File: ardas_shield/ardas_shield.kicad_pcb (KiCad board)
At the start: 2 copper layers, 68.6 x 53.3 mm, 40 parts, among them CON1 SD_Card, IC1 DS1307, P1 CONN_10, P10 CONN_01X03, P2 CONN_8, P3 CONN_8, P4 CONN_ICSP, P5 CONN_6, P6 TTL_COMM, P7 CONN_01X03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

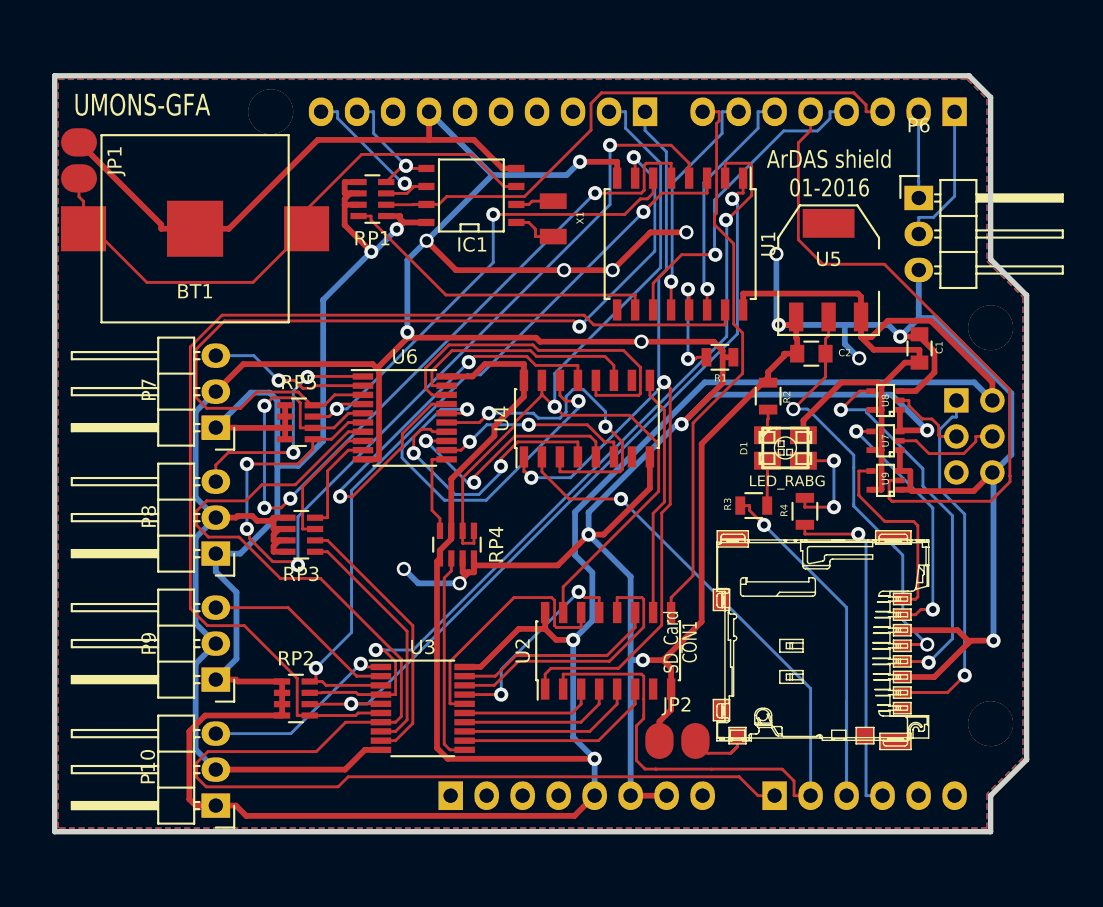
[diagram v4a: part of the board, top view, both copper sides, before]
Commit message: updated SD card and RGB-LED
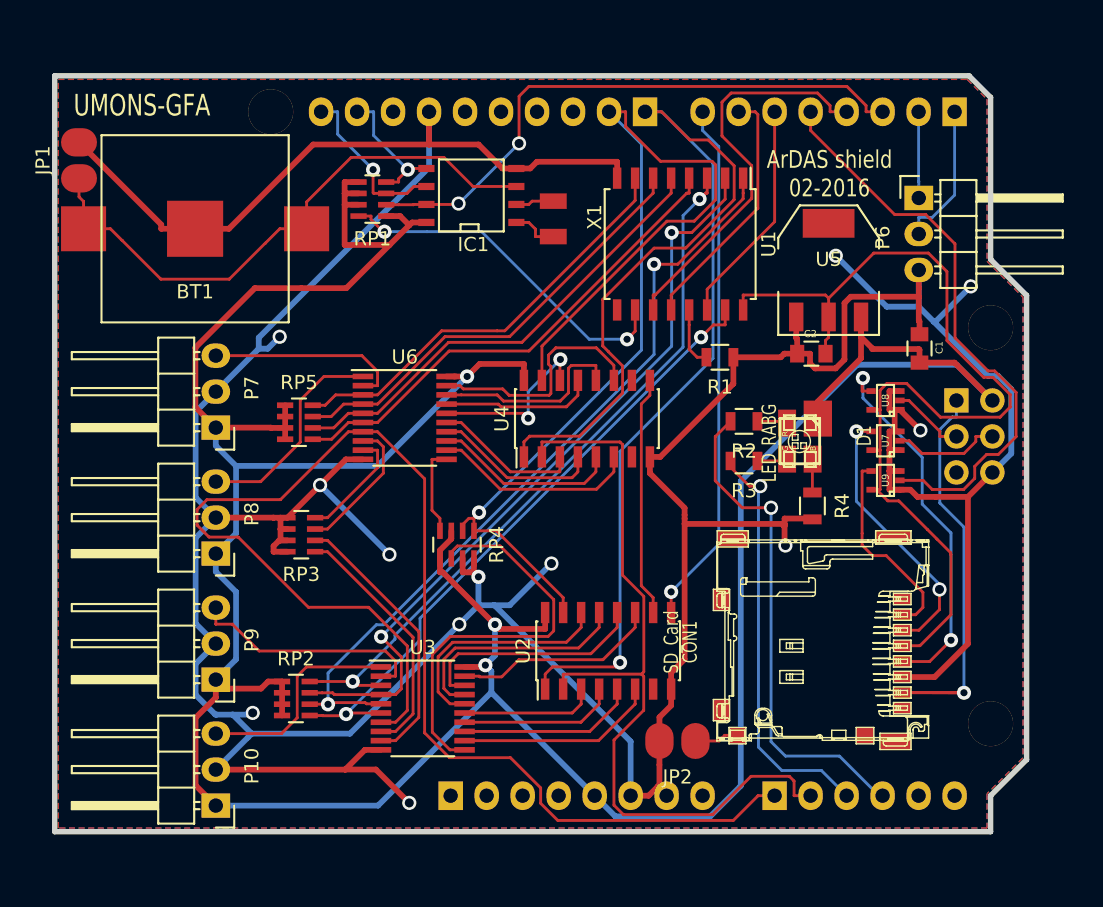
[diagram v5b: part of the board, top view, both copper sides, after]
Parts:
- BT1: footprint MyFootprints:BATTERY_KEYSTONE_12mm -> kicad-gfa local:BATTERY_KEYSTONE_12mm
- C1, C2: footprint Capacitors_SMD:C_0805 -> kicad-gfa local:C_0805
- D1: footprint MyFootprints:led-P-LCC-4-3 -> kicad-gfa local:led-P-LCC-4-3
- IC1: footprint SMD_Packages:SOIC-8-N -> kicad-gfa local:SOIC-8-N
- JP1, JP2: footprint RTC_Ardas_test:small_no_jumper -> kicad-gfa local:small_no_jumper
- P1: footprint Pin_Headers:Pin_Header_Straight_1x10 -> kicad-gfa local:Pin_Header_Straight_1x10
- P10, P6, P7, P8, P9: footprint Pin_Headers:Pin_Header_Angled_1x03 -> kicad-gfa local:Pin_Header_Angled_1x03
- P2, P3: footprint Pin_Headers:Pin_Header_Straight_1x08 -> kicad-gfa local:Pin_Header_Straight_1x08
- P4: footprint Socket_Strips:Socket_Strip_Straight_2x03 -> kicad-gfa local:Socket_Strip_Straight_2x03
- P5: footprint Pin_Headers:Pin_Header_Straight_1x06 -> kicad-gfa local:Pin_Header_Straight_1x06
- R1: footprint Resistors_SMD:R_0805 -> kicad-gfa local:R_0805
- R2: value 150 -> 4.7k; footprint Ardas_shield:R_0805 -> kicad-gfa local:R_0805
- R3: value 100 -> 10k; footprint Ardas_shield:R_0805 -> kicad-gfa local:R_0805
- R4: value 100 -> 4.7k; footprint Ardas_shield:R_0805 -> kicad-gfa local:R_0805
- U1: footprint Housings_SOIC:SOIC-16_7.5x10.3mm_Pitch1.27mm -> kicad-gfa local:SOIC-16_7.5x10.3mm_Pitch1.27mm
- U2, U4: footprint Housings_SOIC:SOIC-16_3.9x9.9mm_Pitch1.27mm -> kicad-gfa local:SOIC-16_3.9x9.9mm_Pitch1.27mm
- U3, U6: footprint Housings_SSOP:TSSOP-20_4.4x6.5mm_Pitch0.65mm -> kicad-gfa local:TSSOP-20_4.4x6.5mm_Pitch0.65mm
- U5: footprint TO_SOT_Packages_SMD:SOT-223 -> kicad-gfa local:SOT-223
- U7, U8, U9: footprint TO_SOT_Packages_SMD:SC-70-5 -> kicad-gfa local:SC-70-5
- X1: footprint MyFootprints:XTAL_ABRACON_ABS07 -> kicad-gfa local:XTAL_ABRACON_ABS07
- moved R3 3.22 mm to (95.7, 95.4)
- moved R2 2.46 mm to (95.7, 92.6), turned to 180 degrees
- moved D1 1.12 mm to (99.6, 94.0), turned to 180 degrees
- moved R4 0.66 mm to (100.5, 98.5)
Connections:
- C2 pad 1: /+3.3V -> +3.3V
- CON1 pad 1: /SEN3 -> (no net)
- CON1 pad 2: /MOSI3 -> /SEN3
- CON1 pad 3: GND -> /MOSI3
- CON1 pad 4: /+3.3V -> +3.3V
- CON1 pad 8: Net-(CON1-Pad8) -> (no net)
- D1 pad 1: Net-(D1-Pad1) -> +5V
- D1 pad 2: +5V -> Net-(D1-Pad2)
- P1 pad 3: Net-(P1-Pad3) -> (no net)
- P1 pad 4: Net-(P1-Pad4) -> (no net)
- P1 pad 5: Net-(P1-Pad5) -> (no net)
- P1 pad 6: Net-(P1-Pad6) -> (no net)
- P1 pad 8: Net-(P1-Pad8) -> (no net)
- P2 pad 1: Net-(P2-Pad1) -> (no net)
- P2 pad 2: Net-(P2-Pad2) -> (no net)
- P2 pad 3: Net-(P2-Pad3) -> (no net)
- P2 pad 4: Net-(P2-Pad4) -> (no net)
- P2 pad 8: Net-(P2-Pad8) -> (no net)
- P4 pad 5: Net-(P4-Pad5) -> (no net)
- P5 pad 5: Net-(P5-Pad5) -> (no net)
- P5 pad 6: Net-(P5-Pad6) -> (no net)
- R2 pad 1: Net-(D1-Pad1) -> Net-(D1-Pad4)
- R2 pad 2: GND -> D17
- R3 pad 1: Net-(D1-Pad4) -> Net-(D1-Pad3)
- R4 pad 1: Net-(D1-Pad3) -> Net-(D1-Pad2)
- R4 pad 2: D17 -> GND
- U1 pad 16: +5V -> +3.3V
- U1 pad 9: Net-(U1-Pad9) -> (no net)
- U2 pad 7: Net-(U2-Pad7) -> (no net)
- U4 pad 10: Net-(U4-Pad10) -> (no net)
- U4 pad 7: Net-(U4-Pad7) -> (no net)
- U5 pad 2: /+3.3V -> +3.3V
- U7 pad 5: +5V -> +3.3V
- U8 pad 5: +5V -> +3.3V
- U9 pad 5: +5V -> +3.3V
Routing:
- net +3.3V: track 0.00 -> 68.6 mm
- net GND: track 395.2 -> 340.8 mm, vias 18 -> 12
- net +5V: track 283.0 -> 239.7 mm, vias 4 -> 3
- net Net-(RP2-Pad5): track 76.6 -> 45.2 mm, vias 0 -> 2
- net Net-(RP5-Pad8): track 61.0 -> 30.3 mm, vias 2 -> 0
- net Net-(RP5-Pad5): track 65.3 -> 34.8 mm, vias 4 -> 0
- net /+3.3V: track 30.4 -> 0.00 mm, vias 2 -> 0
- net D08: track 62.4 -> 90.0 mm, vias 2 -> 1
- net Net-(RP5-Pad6): track 57.6 -> 33.2 mm, vias 4 -> 0
- net Net-(U4-Pad13): track 33.2 -> 10.7 mm, vias 2 -> 0
- net Net-(U4-Pad14): track 27.4 -> 12.5 mm
- net Net-(RP4-Pad6): track 14.9 -> 29.2 mm
- net Net-(U4-Pad3): track 23.9 -> 10.5 mm, vias 2 -> 0
- net Net-(U4-Pad12): track 25.7 -> 13.8 mm
- net D09: track 66.0 -> 77.2 mm
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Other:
- board text added: "ArDAS shield 02-2016"
- board text removed: "ArDAS shield 01-2016"

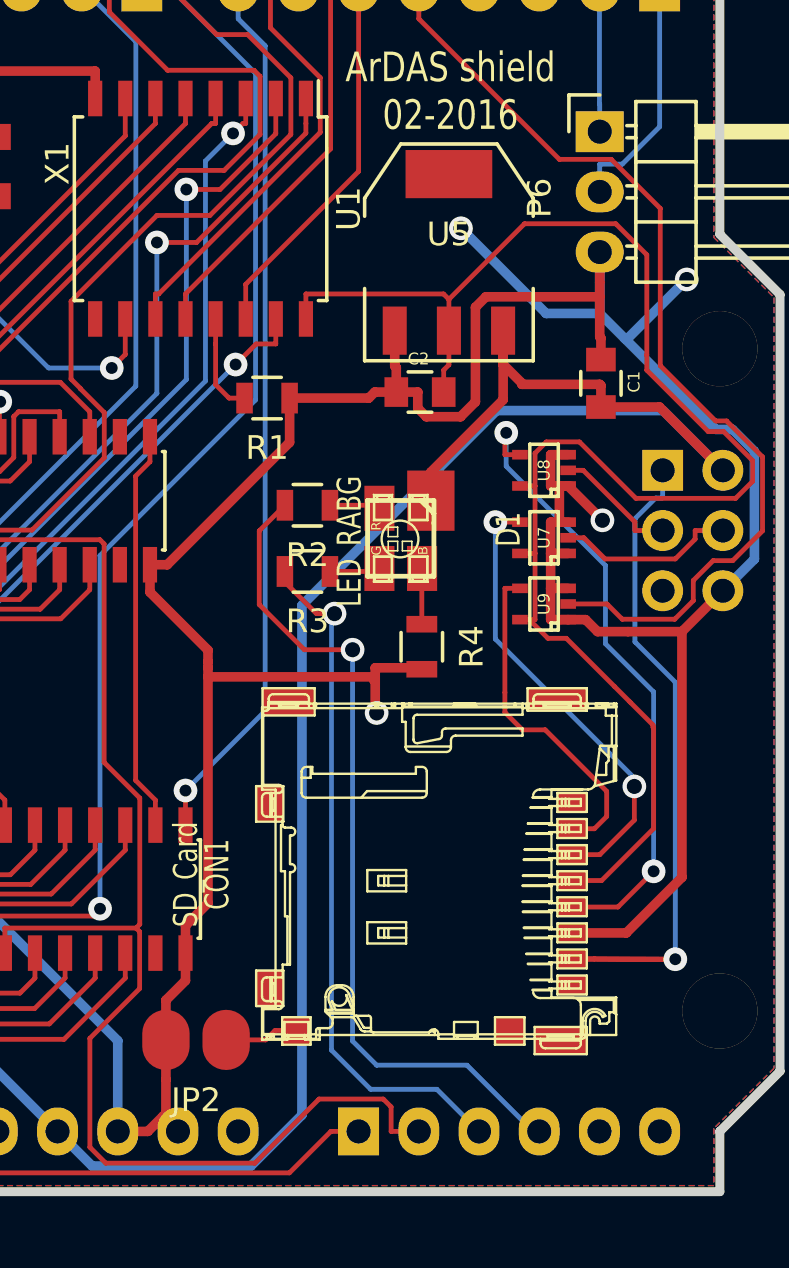
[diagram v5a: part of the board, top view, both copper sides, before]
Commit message: remove sd card components
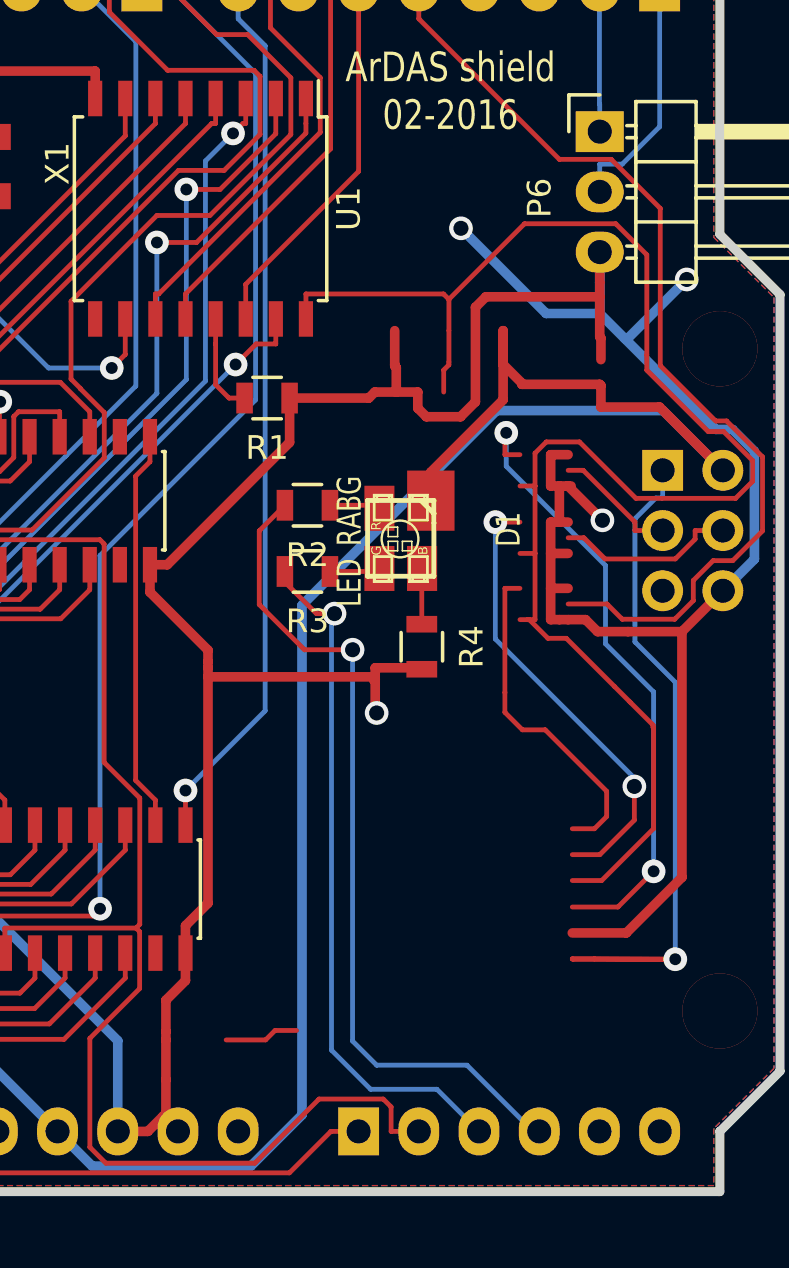
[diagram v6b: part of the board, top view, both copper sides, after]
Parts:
- removed C1, C2: 47uF, kicad-gfa local:C_0805
- removed CON1: SD_Card, kicad-gfa local:microSD_socket
- removed JP2: Jumper_NO_Small, kicad-gfa local:small_no_jumper
- removed U5: LD1117S33TR, kicad-gfa local:SOT-223
- removed U7, U8, U9: 74LVC1G125, kicad-gfa local:SC-70-5
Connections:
- P3 pad 5: D04 -> (no net)
- P4 pad 1: MISO -> (no net)
- P4 pad 3: SCK -> (no net)
- P4 pad 4: MOSI -> (no net)
- U1 pad 16: +3.3V -> (no net)
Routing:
- net (no net): track 0.00 -> 216.5 mm, vias 0 -> 5
- net +3.3V: track 68.6 -> 0.00 mm
- net D04: track 41.0 -> 0.00 mm
- net MISO: track 30.7 -> 0.00 mm, vias 1 -> 0
- net /SCK3: track 26.7 -> 0.00 mm, vias 2 -> 0
- net /MOSI3: track 19.3 -> 0.00 mm, vias 2 -> 0
- net /SEN3: track 14.3 -> 0.00 mm
- net MOSI: track 7.61 -> 0.00 mm
- net SCK: track 5.25 -> 0.00 mm
- net Net-(CON1-PadCD1): track 3.13 -> 0.00 mm

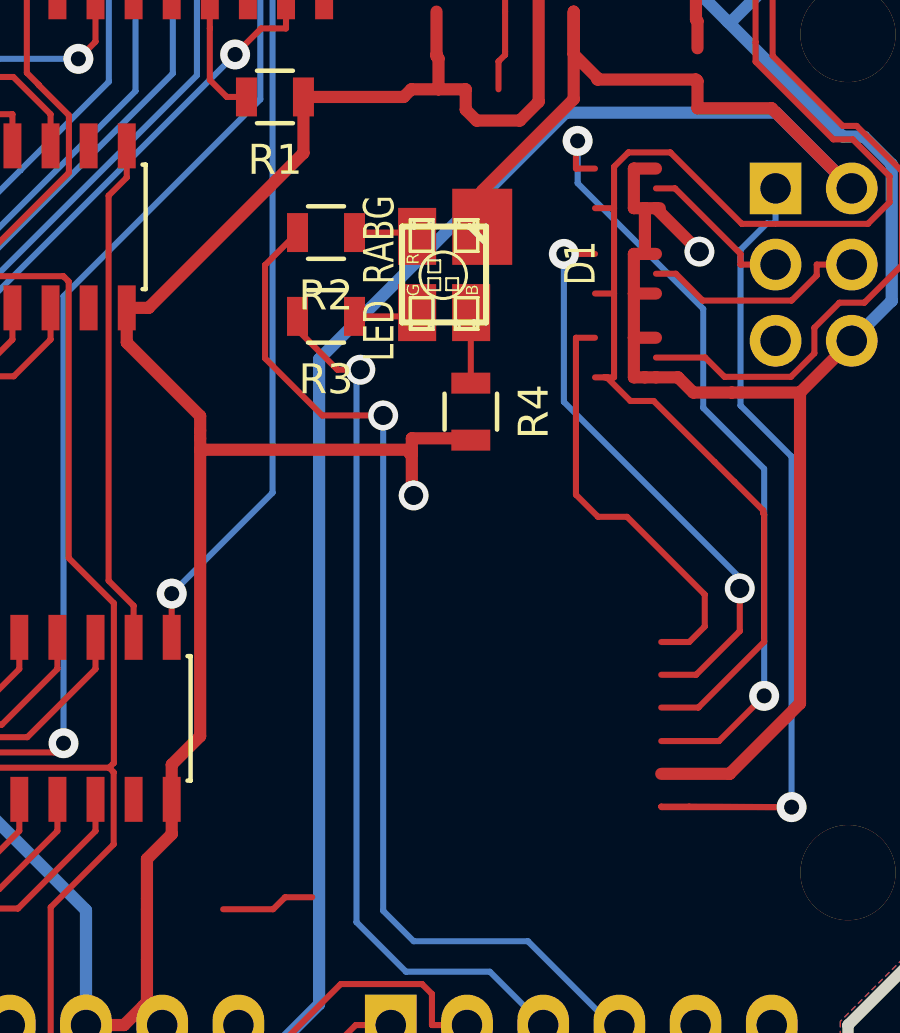
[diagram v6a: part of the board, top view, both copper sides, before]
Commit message: add new leds and footprints
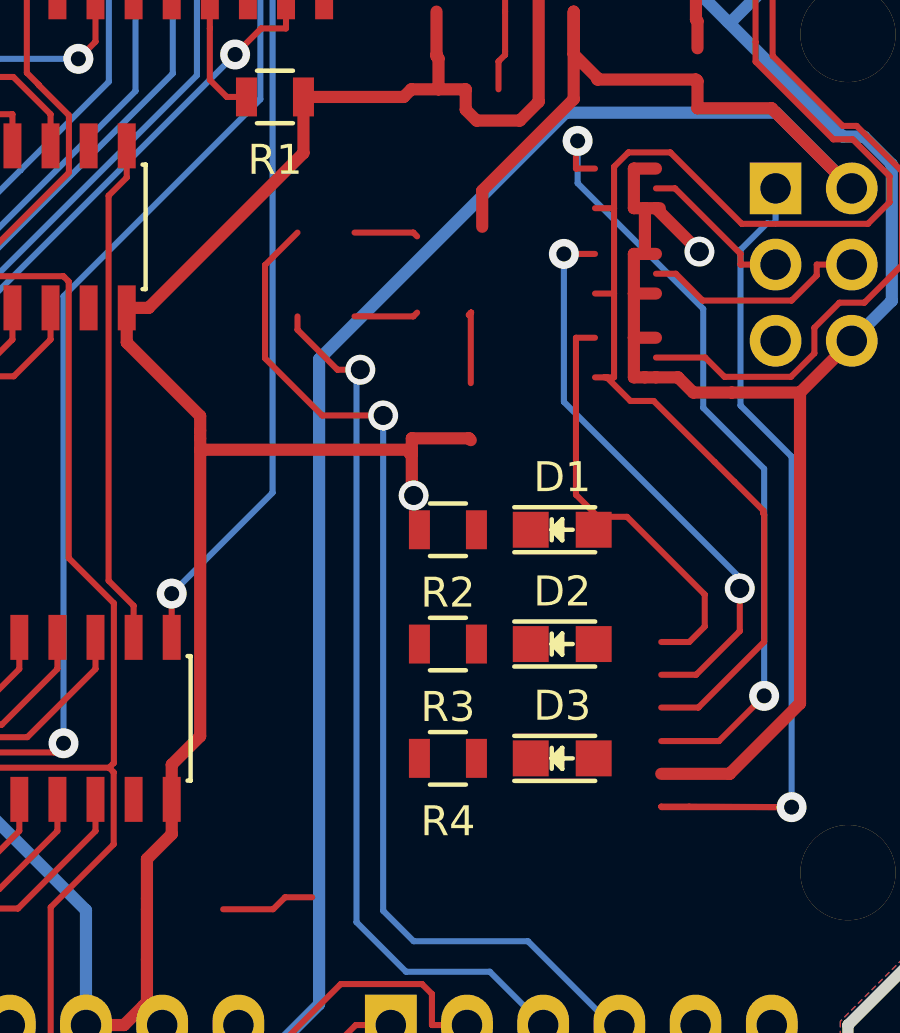
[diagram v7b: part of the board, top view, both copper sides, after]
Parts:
- added D2: LED Yellow, LEDs:LED_0805, F.Cu at (103.6, 106.3)
- added D3: LED Red, LEDs:LED_0805, F.Cu at (103.6, 110.1)
- D1: value LED_RABG -> LED; footprint kicad-gfa local:led-P-LCC-4-3 -> LEDs:LED_0805
- R2: value 4.7k -> 150 Ohm
- R3: value 10k -> 150 Ohm
- R4: value 4.7k -> 160 Ohm
- moved R3 11.7 mm to (99.8, 106.3)
- moved R4 11.6 mm to (99.8, 110.1), turned to 180 degrees
- moved R2 10.7 mm to (99.8, 102.5)
- moved D1 9.38 mm to (103.6, 102.5), turned to 0 degrees
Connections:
- D1 pad 1: +5V -> Net-(D1-Pad1)
- D1 pad 2: Net-(D1-Pad2) -> +5V
- R2 pad 1: Net-(D1-Pad4) -> Net-(D1-Pad1)
- R3 pad 1: Net-(D1-Pad3) -> Net-(D2-Pad1)
- R4 pad 1: Net-(D1-Pad2) -> Net-(D3-Pad1)
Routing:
- net +5V: track 239.7 -> 254.0 mm
- net (no net): track 216.5 -> 209.0 mm
- net Net-(D1-Pad2): track 2.57 -> 0.00 mm
- net Net-(D1-Pad4): track 2.14 -> 0.00 mm
- net Net-(D1-Pad3): track 2.14 -> 0.00 mm

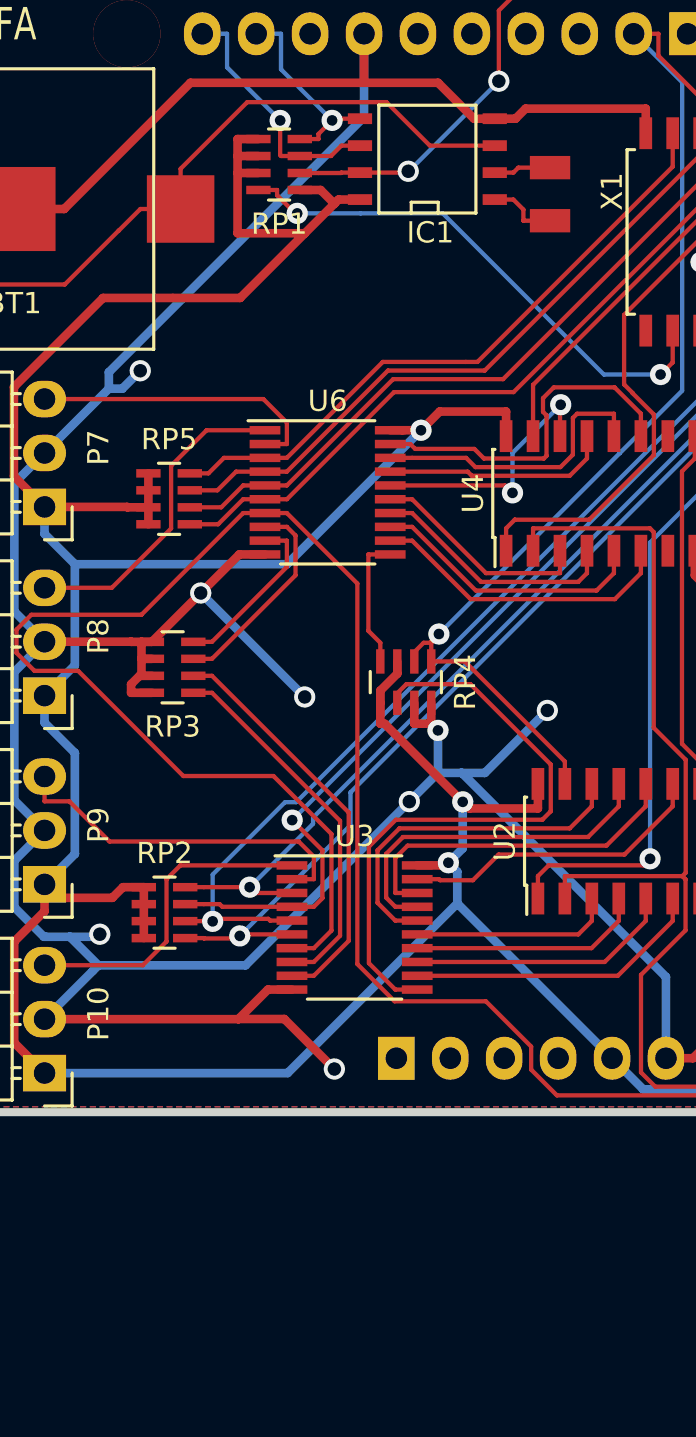
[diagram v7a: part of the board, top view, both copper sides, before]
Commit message: complete componenents metadatas with Kifield
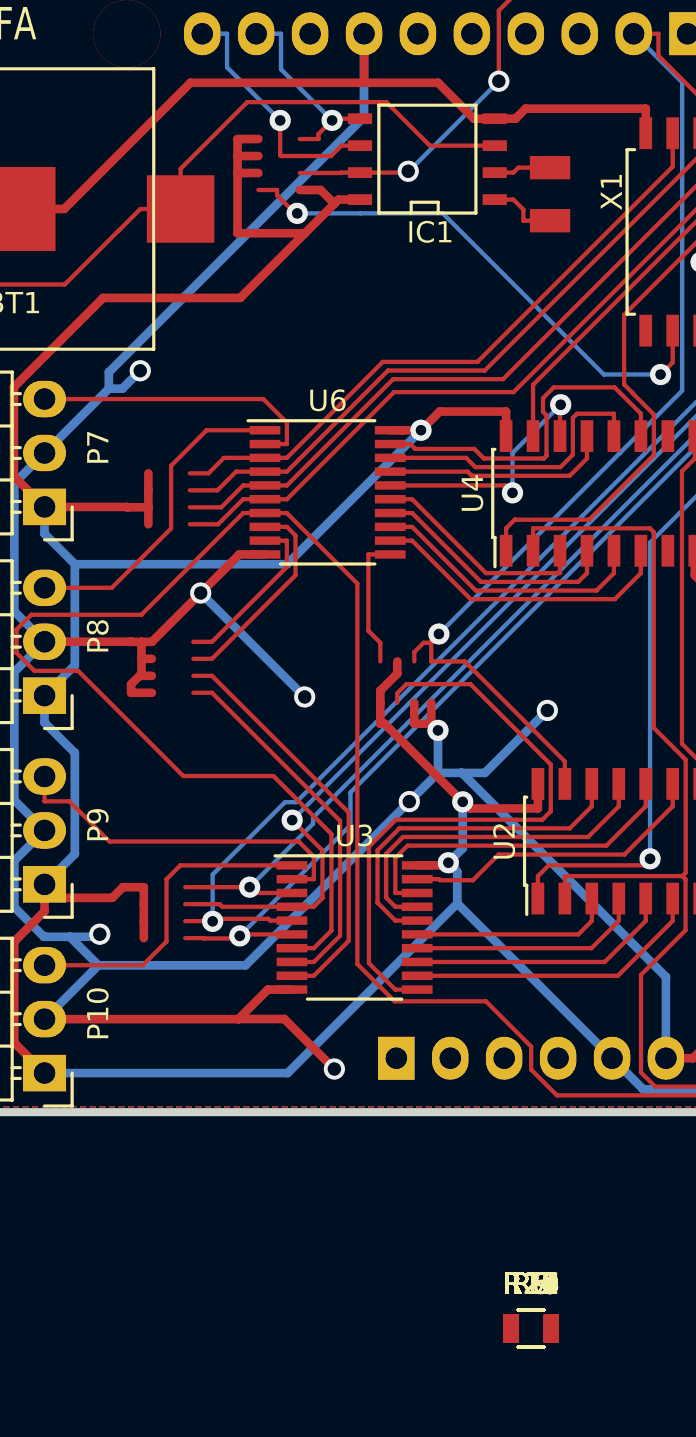
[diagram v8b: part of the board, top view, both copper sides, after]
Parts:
- removed RP1: R_4x4.7k, kicad-gfa local:R_Array_Convex_4x0603
- removed RP2, RP3, RP4, RP5: R_4x10k, kicad-gfa local:R_Array_Convex_4x0603
- added R10, R11, R12, R13, R14, R15, R16, R17, R18, R19, R20, R21, R22, R23, R24, R9: R_10K, Resistors_SMD:R_0805, F.Cu at (81.3, 131.7)
- added R5, R6, R7, R8: R_4.7K, Resistors_SMD:R_0805, F.Cu at (81.3, 131.7)
